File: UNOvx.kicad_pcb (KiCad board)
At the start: 2 copper layers, 72 x 53.5 mm, 38 parts, among them IC1 BTS462T, J1 Barrel_Jack_Switch, J2 Ext. Power, J3 Conn_01x02_Male, J4 Conn_02x03_Odd_Even, P1 Analog, P2 Power, P3 Digital, P4 Digital, P5 CONN_01X01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

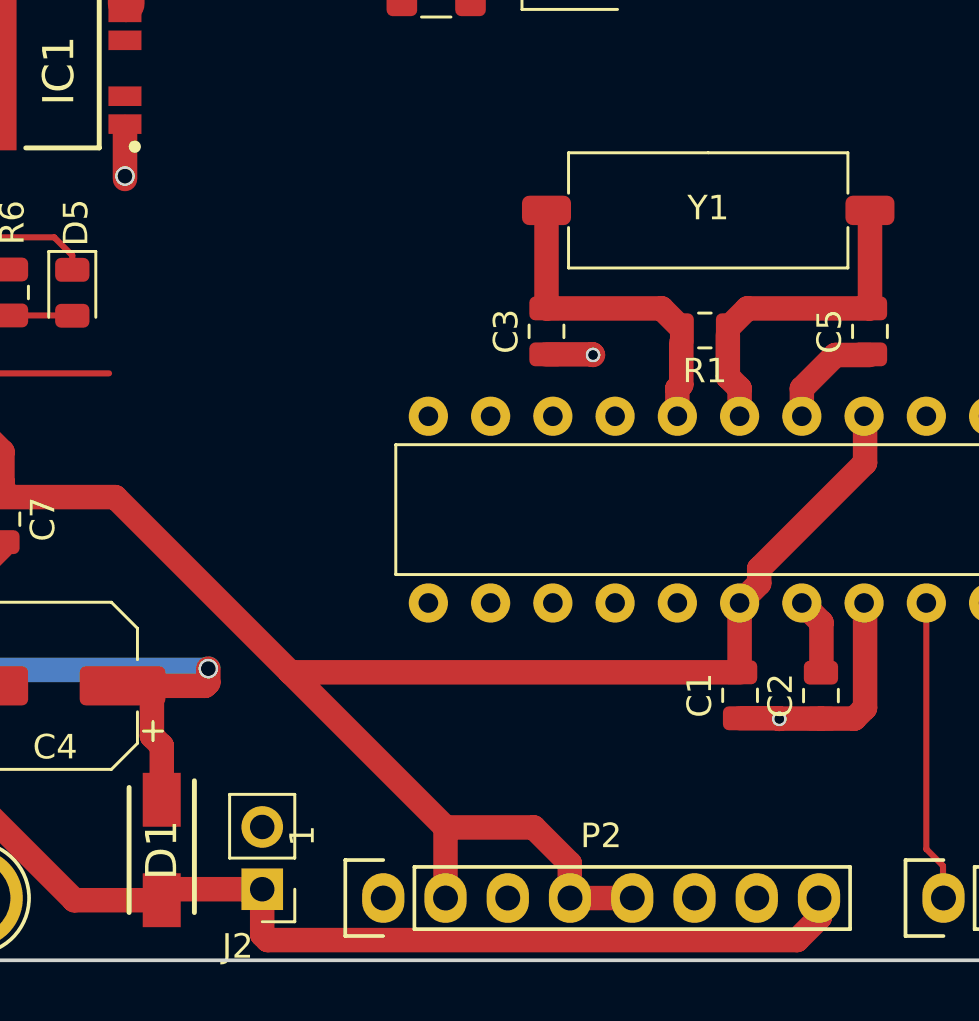
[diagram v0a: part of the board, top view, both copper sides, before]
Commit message: No power connector
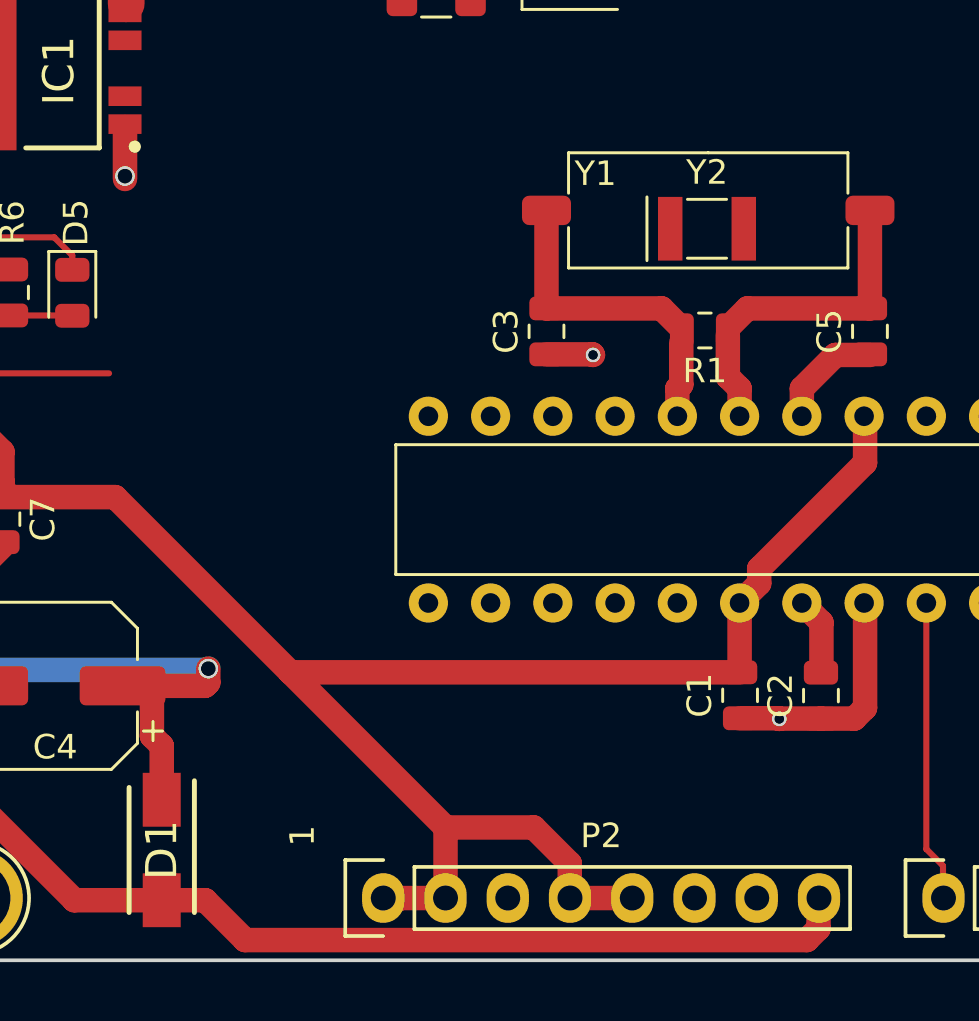
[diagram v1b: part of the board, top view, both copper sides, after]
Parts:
- removed J2: Ext. Power, Connector_PinHeader_2.54mm:PinHeader_1x02_P2.54mm_Vertical
- added Y2: 16MHz, Crystal:Resonator_SMD_muRata_CDSCB-2Pin_4.5x2.0mm, F.Cu at (155.4, 96.5)
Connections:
- P2 pad 1: Net-(P2-Pad1) -> +5V
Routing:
- net +5V: track 92.9 -> 95.5 mm
- net Vin: track 43.8 -> 42.5 mm

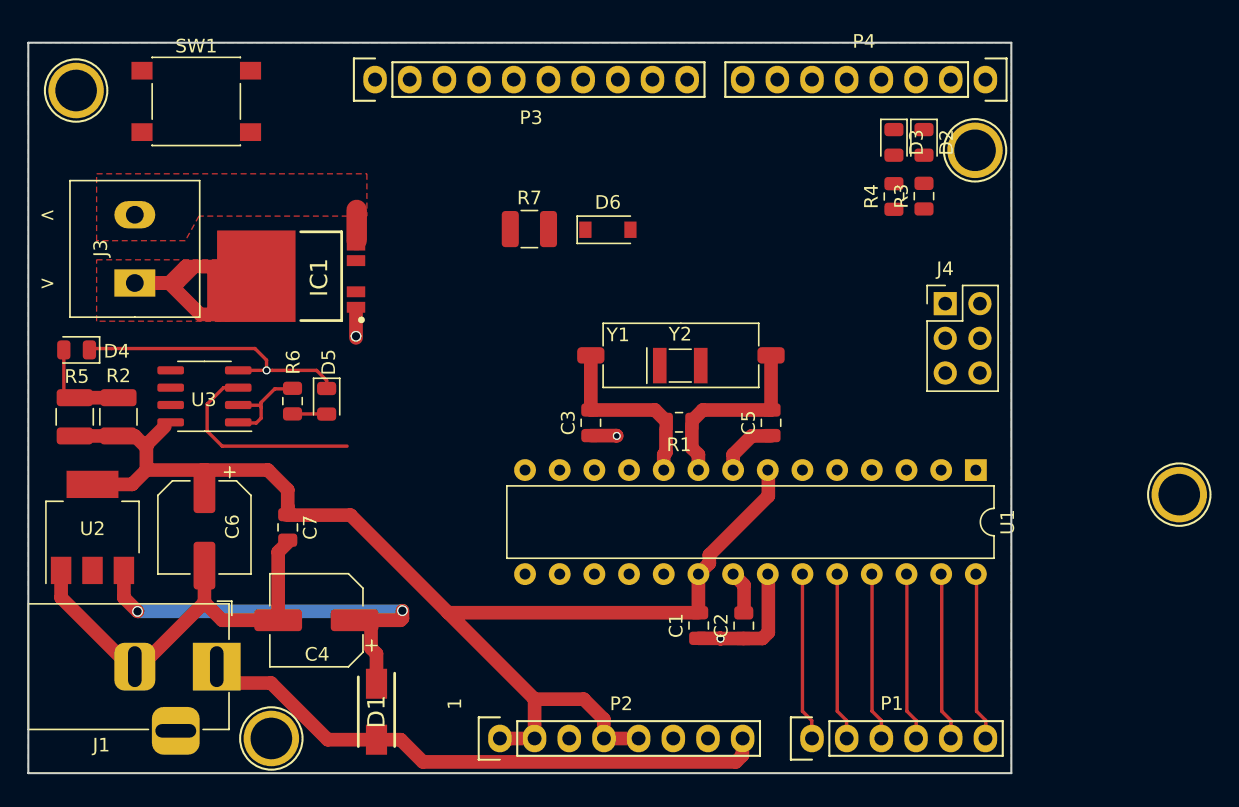
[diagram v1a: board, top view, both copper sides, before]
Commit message: Move the chip to allow hole
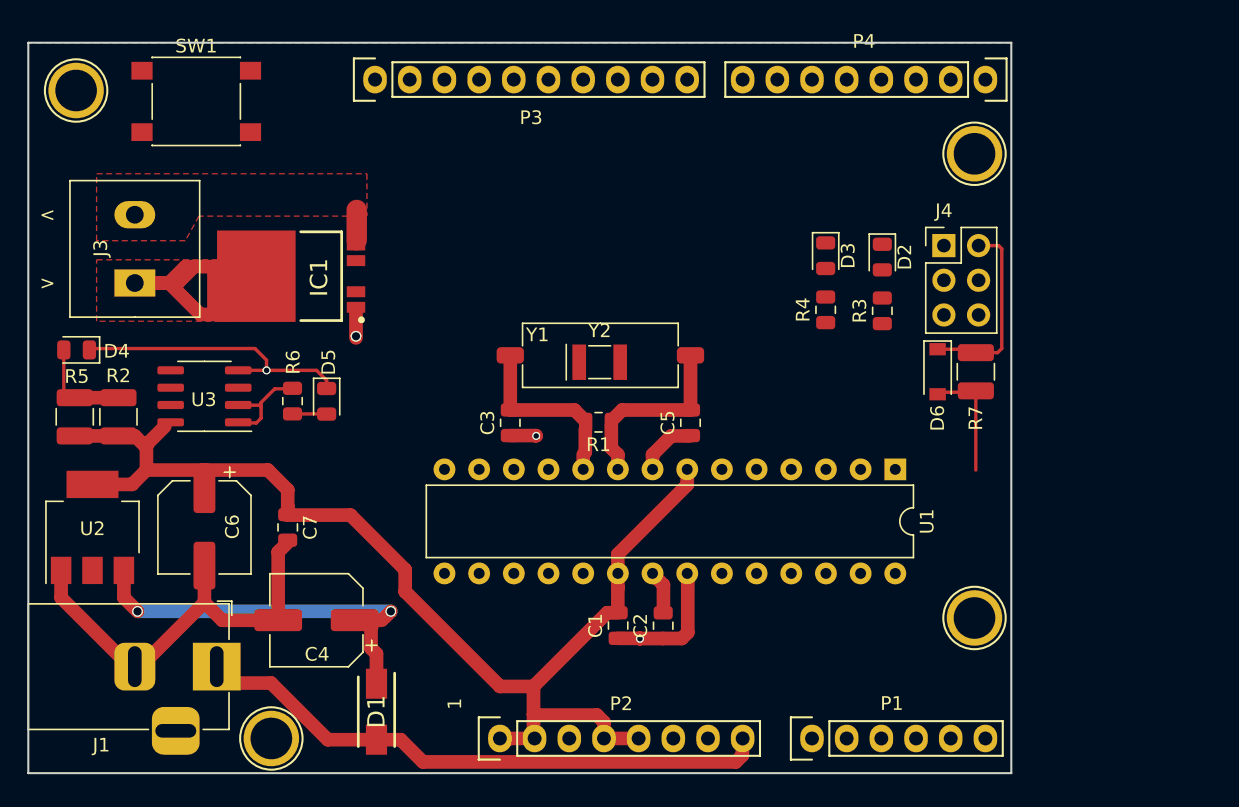
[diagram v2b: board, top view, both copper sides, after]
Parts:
- moved R7 34.3 mm to (177.1, 97.0), turned to 270 degrees
- moved D6 26.3 mm to (174.3, 97.0), turned to 270 degrees
- moved P6 17.5 mm to (177.0, 115.0)
- moved D3 9.69 mm to (166.1, 88.5)
- moved R4 9.69 mm to (166.1, 92.4)
- moved D2 8.94 mm to (170.2, 88.6)
- moved R3 8.94 mm to (170.2, 92.5)
- moved Y2 5.91 mm to (149.5, 96.3)
- moved U1 5.90 mm to (171.2, 104.1)
- moved C1 5.90 mm to (150.9, 115.6)
- moved C2 5.90 mm to (154.2, 115.6)
- moved C3 5.90 mm to (143.0, 100.7)
- moved C5 5.90 mm to (156.2, 100.7)
- moved R1 5.90 mm to (149.5, 100.7)
- moved Y1 5.90 mm to (149.6, 95.8)
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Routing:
- net PB5(SCK): track 15.5 -> 0.00 mm
- net A5(SCL): track 12.3 -> 0.00 mm
- net A3: track 12.3 -> 0.00 mm
- net A2: track 12.3 -> 0.00 mm
- net A0: track 12.3 -> 0.00 mm
- net A4(SDA): track 13.2 -> 0.87 mm
- net A1: track 12.3 -> 0.00 mm
- net Reset: track 0.00 -> 8.50 mm
- net +5V: track 95.5 -> 99.4 mm
- net Net-(C4-Pad1): track 30.5 -> 29.4 mm

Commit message: Add lines
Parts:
- moved D6 6.85 mm to (177.6, 103.0), turned to 90 degrees
- moved R7 6.37 mm to (174.7, 102.9), turned to 90 degrees
- moved P5 0.50 mm to (125.0, 123.8)
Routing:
- net Rx: track 0.00 -> 38.7 mm
- net Tx: track 0.00 -> 36.6 mm
- net PD4: track 0.00 -> 32.3 mm
- net PD3: track 0.00 -> 32.3 mm
- net PD2: track 0.00 -> 32.3 mm
- net +5V: track 99.4 -> 110.3 mm
- net Reset: track 8.50 -> 16.7 mm
- net Net-(D2-Pad2): track 0.00 -> 1.91 mm
- net Net-(D3-Pad2): track 0.00 -> 1.86 mm

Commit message: More lines
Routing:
- net AREF: track 3.14 -> 74.6 mm
- net A4(SDA): track 0.87 -> 71.0 mm
- net A5(SCL): track 0.00 -> 66.7 mm
- net PD6: track 0.00 -> 39.8 mm, vias 0 -> 1
- net PD5: track 0.00 -> 39.8 mm, vias 0 -> 1
- net +5V: track 110.3 -> 133.4 mm, vias 0 -> 3
- net A1: track 0.00 -> 14.8 mm
- net A0: track 0.00 -> 14.8 mm
- net A3: track 0.00 -> 14.8 mm
- net A2: track 0.00 -> 14.8 mm
- added copper zone on F.Cu, net GND

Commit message: All except GND plane
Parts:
- moved J4 6.26 mm to (177.1, 93.5), turned to 180 degrees
- moved D5 1.92 mm to (128.5, 97.5), turned to 0 degrees
- moved R6 1.71 mm to (128.5, 100.0), turned to 0 degrees
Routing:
- net PB5(SCK): track 0.00 -> 121.3 mm, vias 0 -> 2
- net PB3(MOSI): track 0.00 -> 115.2 mm
- net Reset: track 16.7 -> 130.1 mm, vias 0 -> 4
- net PB4(MISO): track 0.00 -> 97.4 mm
- net PD7: track 0.00 -> 48.7 mm, vias 0 -> 2
- net PB2(SS): track 0.00 -> 41.7 mm
- net PB1(9): track 0.00 -> 38.6 mm
- net PB0(8): track 0.00 -> 36.7 mm, vias 0 -> 1
- net +5V: track 133.4 -> 155.4 mm, vias 3 -> 4
- net XTAL1: track 13.5 -> 17.1 mm
- net XTAL2: track 12.5 -> 15.2 mm
- net GND: track 69.9 -> 67.3 mm, vias 4 -> 6
- net Net-(R6-Pad1): track 5.81 -> 7.21 mm
- net A4(SDA): track 71.0 -> 70.5 mm
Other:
- net class Default: clearance 0.2 -> 0.3
- net class Signal: clearance 0.2 -> 0.4
- rule trace_clearance: 0.2 -> 0.3

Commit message: 4 layers
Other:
- copper layers 2 -> 4
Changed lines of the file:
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@@
   )
   (layers
-    (0 F.Cu signal)
+    (0 F.Cu mixed)
+    (1 In1.Cu signal)
+    (2 In2.Cu signal)
     (31 B.Cu power)
-    (32 B.Adhes user)
-    (33 F.Adhes user)
     (34 B.Paste user)
     (35 F.Paste user)
@@
     (40 Dwgs.User user)
     (41 Cmts.User user)
-    (42 Eco1.User user)
-    (43 Eco2.User user)
     (44 Edge.Cuts user)
     (45 Margin user)

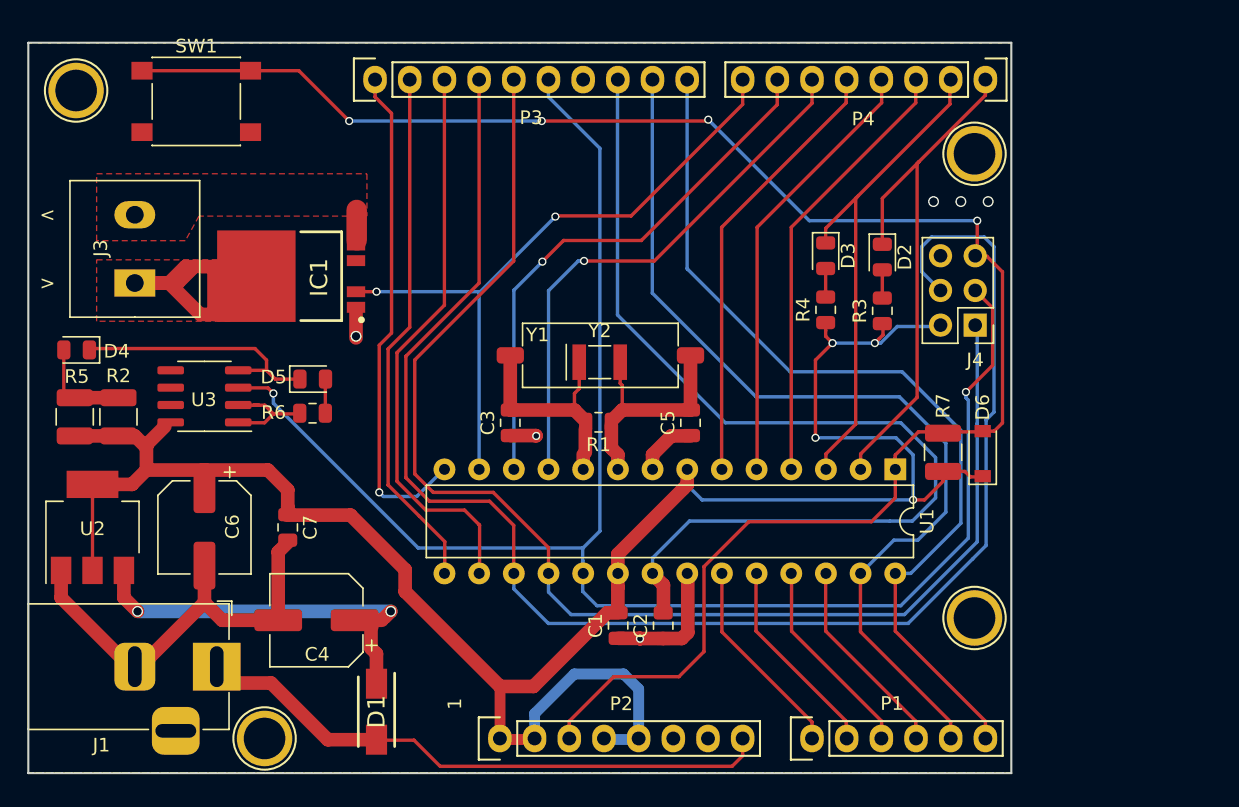
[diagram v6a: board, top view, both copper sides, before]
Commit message: Layout in 2 layers
No diodes for Rx,Tx
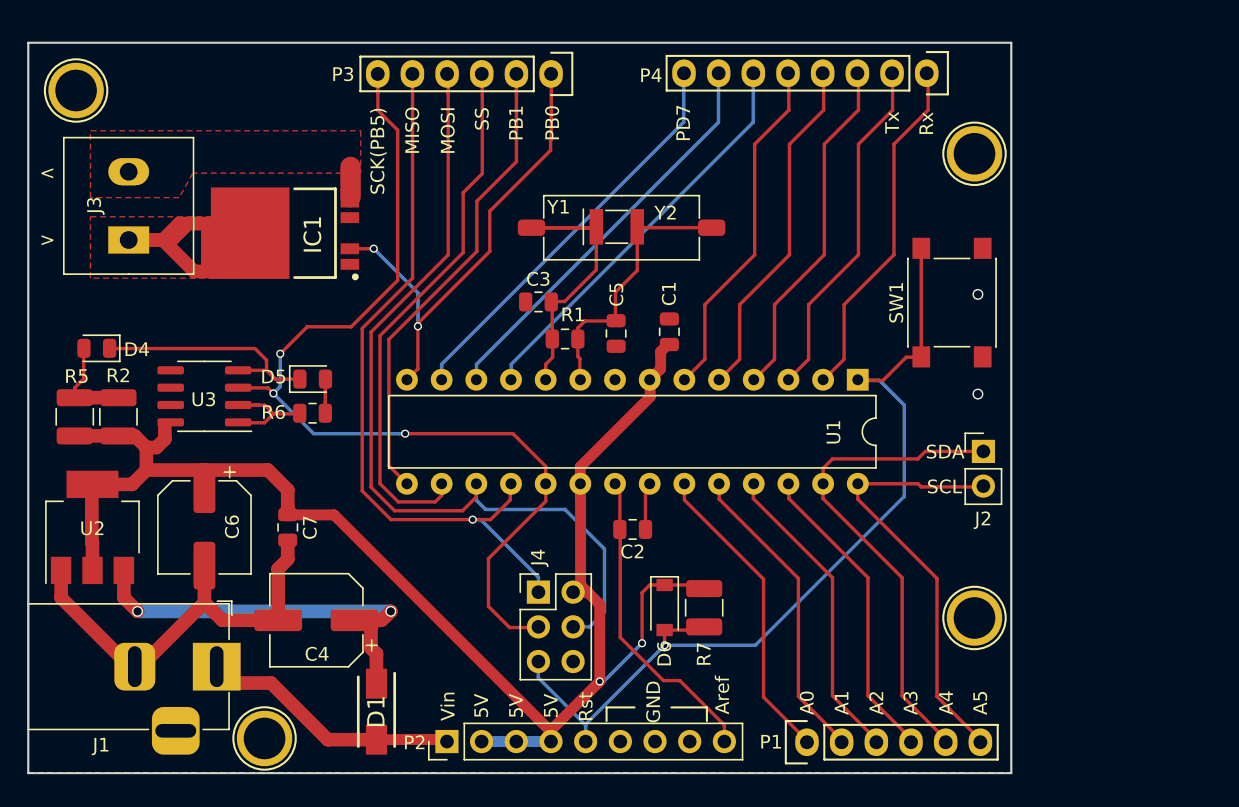
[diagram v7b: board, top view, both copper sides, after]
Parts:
- removed D2, D3: Yellow, LED_SMD:LED_0805_2012Metric
- removed R3, R4: 1k, Resistor_SMD:R_0805_2012Metric
- added J2: I2C/TWI, Connector_PinHeader_2.54mm:PinHeader_1x02_P2.54mm_Vertical, F.Cu at (177.7, 102.8)
- P1: value Analog -> Analog PC
- P2: footprint Socket_Arduino_Uno:Socket_Strip_Arduino_1x08 -> Connector_PinHeader_2.54mm:PinHeader_1x09_P2.54mm_Vertical
- P3: value Digital -> Digital PB; footprint Socket_Arduino_Uno:Socket_Strip_Arduino_1x10 -> Socket_Arduino_Uno:Socket_Strip_Arduino_1x06
- P4: value Digital -> Digital PD
- moved SW1 57.3 mm to (175.3, 91.9), turned to 90 degrees
- moved J4 37.5 mm to (145.1, 113.1), turned to 0 degrees
- moved D6 25.9 mm to (154.3, 114.2), turned to 270 degrees
- moved C1 21.8 mm to (154.7, 94.0), turned to 270 degrees
- moved R7 20.9 mm to (157.2, 114.2), turned to 270 degrees
- moved P3 12.9 mm to (146.0, 75.2), turned to 180 degrees
- moved Y2 9.99 mm to (150.8, 86.3)
- moved Y1 9.48 mm to (151.2, 86.4)
- moved C3 9.09 mm to (145.1, 91.8), turned to 0 degrees
- moved C5 8.51 mm to (150.8, 94.2)
- moved C2 7.40 mm to (152.0, 108.5), turned to 180 degrees
- moved U1 7.12 mm to (168.4, 97.5)
- moved R1 6.57 mm to (147.0, 94.6)
- moved P4 4.32 mm to (173.5, 75.1)
- moved P2 3.88 mm to (138.4, 124.0), turned to 90 degrees
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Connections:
- IC1 pad 2: PD7 -> PB0(8)
- P2 pad 1: +5V -> Vin
- P2 pad 3: Reset -> +5V
- P2 pad 5: +5V -> Reset
- P2 pad 8: Vin -> GND
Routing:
- net Reset: track 130.1 -> 64.7 mm, vias 4 -> 1
- net PB3(MOSI): track 115.2 -> 61.7 mm
- net AREF: track 74.6 -> 22.2 mm
- net PB5(SCK): track 121.3 -> 70.5 mm, vias 2 -> 3
- net PB4(MISO): track 97.4 -> 52.9 mm, vias 0 -> 1
- net +5V: track 155.4 -> 111.7 mm, vias 4 -> 2
- net A5(SCL): track 66.7 -> 31.8 mm
- net A4(SDA): track 70.5 -> 36.7 mm
- net Vin: track 42.7 -> 18.9 mm
- net PD7: track 48.7 -> 29.8 mm, vias 2 -> 0
- net GND: track 67.3 -> 51.0 mm, vias 6 -> 2
- net Rx: track 38.7 -> 25.6 mm
- net Tx: track 36.6 -> 25.6 mm
- net PD5: track 39.8 -> 29.8 mm, vias 1 -> 0
- net PD6: track 39.8 -> 30.3 mm, vias 1 -> 0
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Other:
- copper layers 4 -> 2
- board text added: "5V"
- board text added: "A0"
- board text added: "A1"
- board text added: "A2"
- board text added: "A3"
- board text added: "A4"
- board text added: "A5"
- board text added: "Aref"
- board text added: "GND"
- board text added: "MISO"
- board text added: "MOSI"
- board text added: "PB0"
- board text added: "PB1"
- board text added: "PD7"
- board text added: "Rst"
- board text added: "Rx"
- board text added: "SCK(PB5)"
- board text added: "SCL"
- board text added: "SDA"
- board text added: "SS"
- board text added: "Tx"
- board text added: "Vin"
- board text removed: "1"
